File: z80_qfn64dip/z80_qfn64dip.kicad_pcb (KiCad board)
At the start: 4 copper layers, 60 x 24 mm, 49 parts, among them J1 Conn_08, U1 Caravel_QFN, U2 Z80CPU, U3 TPS7A2033PDQNRM3, U4 TPS7A2018PDQNRM3, U5 TPS7A2050PDQNRM3, U6 AT25EU0081A

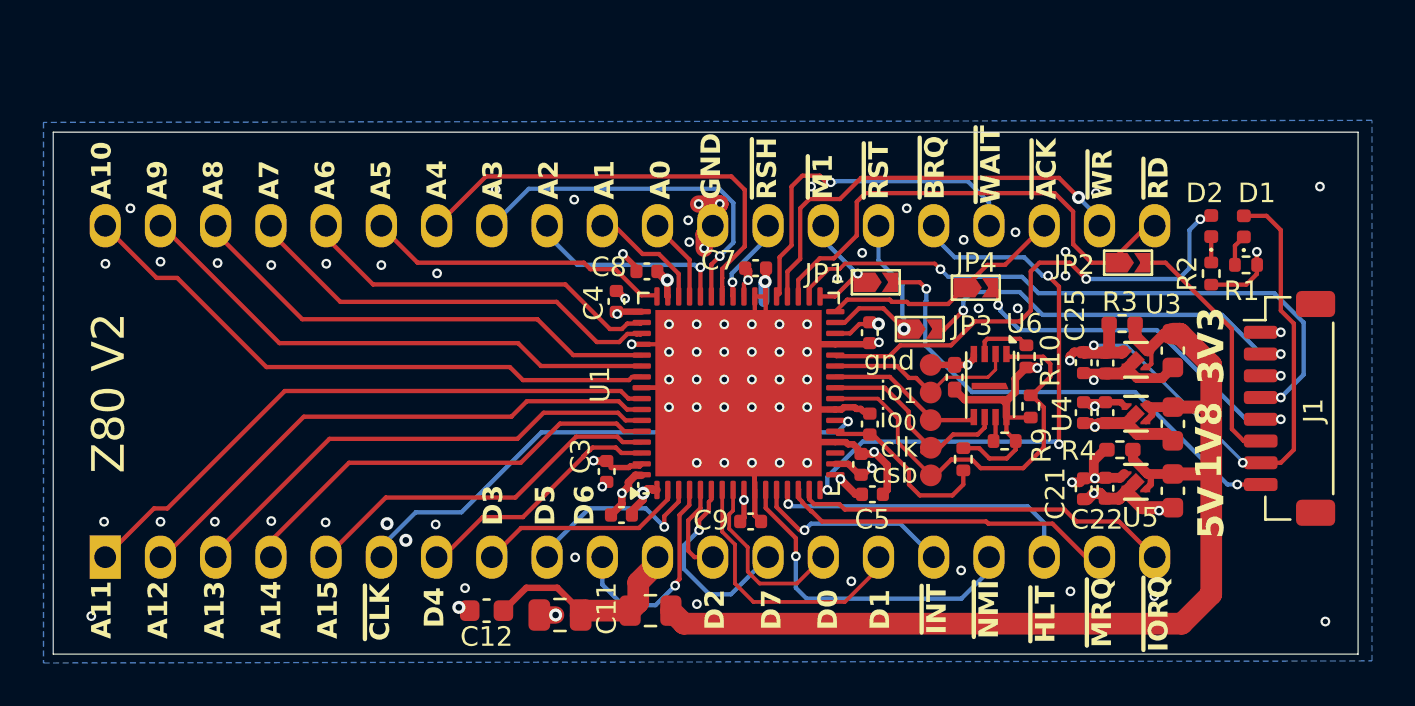
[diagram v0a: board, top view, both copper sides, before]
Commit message: Update mezzanine and Z80 QFN hardware designs
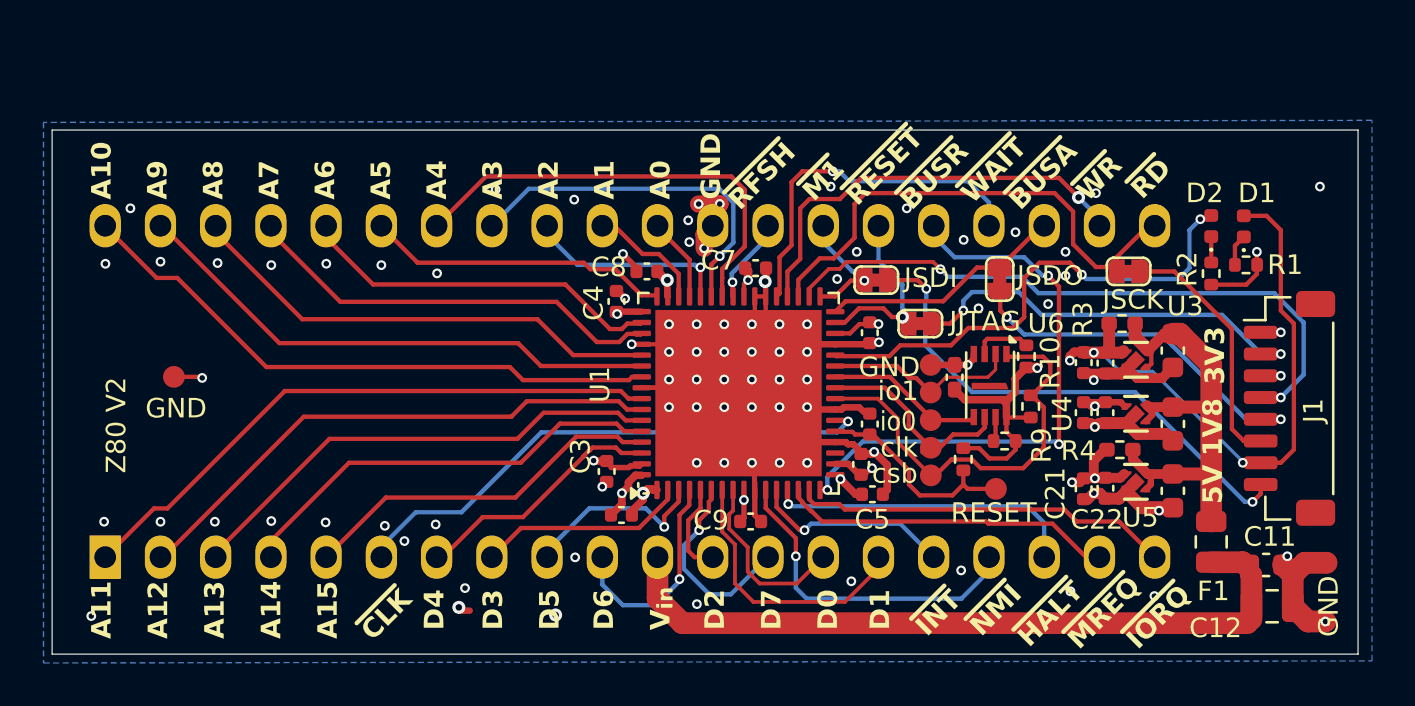
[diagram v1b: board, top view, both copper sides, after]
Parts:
- removed JP4: J_SDO, ProjectLibrary:SolderJumper-2_P2x0.9mm_Open_TrianglePad
- added JP5: JSDO, ProjectLibrary:SolderJumper-2_P1.3mm_Bridged_RoundedPad1.0x1.5mm_Small_Margin, F.Cu at (160.0, 78.3)
- added TP14: RESET, ProjectLibrary:TestPoint_Pad_D1.0mm_Small_Margin, F.Cu at (159.8, 87.9)
- added TP15: GND, ProjectLibrary:TestPoint_Pad_D1.0mm_Small_Margin, F.Cu at (122.0, 82.8)
- added TP16: GND, ProjectLibrary:TestPoint_Pad_D1.0mm_Small_Margin, F.Cu at (175.0, 91.3)
- JP1: value J_SDI -> JSDI; footprint ProjectLibrary:SolderJumper-2_P2x0.9mm_Open_TrianglePad -> ProjectLibrary:SolderJumper-2_P1.3mm_Bridged_RoundedPad1.0x1.5mm_Small_Margin
- JP2: value J_SCK -> JSCK; footprint ProjectLibrary:SolderJumper-2_P2x0.9mm_Open_TrianglePad -> ProjectLibrary:SolderJumper-2_P1.3mm_Bridged_RoundedPad1.0x1.5mm_Small_Margin
- JP3: value J_JTAG -> JJTAG; footprint ProjectLibrary:SolderJumper-2_P2x0.9mm_Open_TrianglePad -> ProjectLibrary:SolderJumper-2_P1.3mm_Bridged_RoundedPad1.0x1.5mm_Small_Margin
- R12: value 4k7 -> 10k
- TP10: value io_{0} -> io0
- TP13: value gnd -> GND
- TP9: value io_{1} -> io1
- moved C12 35.9 mm to (172.3, 91.4), turned to 0 degrees
- moved C11 32.7 mm to (172.5, 93.3), turned to 0 degrees
- moved F1 26.0 mm to (169.7, 90.3), turned to 90 degrees
- moved JP2 0.40 mm to (165.9, 77.9)
- moved JP3 0.25 mm to (156.3, 80.3)
- moved JP1 0.10 mm to (154.3, 78.3)
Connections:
- net Net-(J1-Pin_2) renamed /HKJTAG
- net Net-(J1-Pin_6) renamed /HKSCK
- net Net-(J1-Pin_8) renamed /HKSDI
- J1 pad 5: Net-(J1-Pin_5) -> /HKSDO
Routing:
- net /VIN_{F}: track 51.5 -> 22.5 mm
- net /VIN: track 9.92 -> 33.4 mm
- net Net-(J1-Pin_5): track 16.1 -> 0.00 mm, vias 2 -> 0
- net /HKSDO: track 0.00 -> 15.9 mm, vias 0 -> 2
- net GND: track 74.5 -> 80.2 mm, vias 91 -> 93
- net ~{SOC_RST}: track 8.34 -> 9.93 mm
- net HK_SCK: track 22.6 -> 24.0 mm
- net /HKSDI: track 22.4 -> 23.5 mm
- net HK_JTAG: track 9.06 -> 8.18 mm
- net HK_SDI: track 5.06 -> 5.72 mm
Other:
- board size 60 x 24 mm -> 60.1 x 24.1 mm
- board text added: "V_{in}"
- board text added: "~{BUSA}"
- board text added: "~{BUSR}"
- board text added: "~{HALT}"
- board text added: "~{MREQ}"
- board text added: "~{RESET}"
- board text added: "~{RFSH}"
- board text removed: "~{ACK}"
- board text removed: "~{BRQ}"
- board text removed: "~{HLT}"
- board text removed: "~{MRQ}"
- board text removed: "~{RSH}"
- board text removed: "~{RST}"
